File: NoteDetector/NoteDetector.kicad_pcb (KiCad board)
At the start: 2 copper layers, 25 x 25 mm, 24 parts, among them J1 Conn_02x03, J3 Conn_01x01, J4 Conn_01x01, Q1 Q_NMOS_DGS, U1 VM1010, U2 OPAMP, U3 ATtiny1614-SS

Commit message: save work: new layout almost done
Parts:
- removed U3: ATtiny1614-SS, Package_SO:SOIC-14_3.9x8.7mm_P1.27mm
- added C10: 22p, Capacitor_SMD:C_0603_1608Metric, F.Cu at (-3.86, 8.70)
- added C11: 100n, Capacitor_SMD:C_0603_1608Metric, F.Cu at (8.65, 5.25)
- added C12: 10n, Capacitor_SMD:C_0603_1608Metric, F.Cu at (7.15, 5.25)
- added C13: 1u, Capacitor_SMD:C_0603_1608Metric, F.Cu at (-0.75, -3.20)
- added C14: 1u, Capacitor_SMD:C_0603_1608Metric, F.Cu at (-0.75, -7.70)
- added C15: 1u, Capacitor_SMD:C_0603_1608Metric, F.Cu at (2.15, -2.00)
- added C8: 22p, Capacitor_SMD:C_0603_1608Metric, F.Cu at (-0.81, 9.82)
- added C9: 22p, Capacitor_SMD:C_0603_1608Metric, F.Cu at (-3.86, 5.70)
- added J2: Conn_01x01, TestPoint:TestPoint_Pad_D1.0mm, F.Cu at (10.5, 4.85)
- added J5: Conn_01x01, TestPoint:TestPoint_Loop_D2.50mm_Drill1.0mm, F.Cu at (-9.30, 6.40)
- added MK1: Microphone_Condenser, User:ElectretCondenserMic_SMT_MO063602-1, B.Cu at (0.00, 0.00)
- added Q2: Q_NMOS_DGS, Package_TO_SOT_SMD:SOT-23, F.Cu at (4.70, -6.00)
- added Q3: Q_NMOS_DGS, Package_TO_SOT_SMD:SOT-23, F.Cu at (-0.35, -10.2)
- added Q4: Q_NMOS_DGS, Package_TO_SOT_SMD:SOT-23, F.Cu at (3.55, -9.70)
- added R10: 10M, Resistor_SMD:R_0603_1608Metric, F.Cu at (-0.36, 1.12)
- added R11: 270k, Resistor_SMD:R_0603_1608Metric, F.Cu at (0.39, 3.38)
- added R12: 100, Resistor_SMD:R_0603_1608Metric, F.Cu at (5.80, 8.30)
- added R13: 10M, Resistor_SMD:R_0603_1608Metric, F.Cu at (3.39, 3.38)
- added R14: 10M, Resistor_SMD:R_0603_1608Metric, F.Cu at (0.69, 9.82)
- added R15: 270k, Resistor_SMD:R_0603_1608Metric, F.Cu at (-3.14, 11.0)
- added R16: 270k, Resistor_SMD:R_0603_1608Metric, F.Cu at (-2.36, 5.70)
- added R17: 270k, Resistor_SMD:R_0603_1608Metric, F.Cu at (-2.36, 8.70)
- added R18: R, Resistor_SMD:R_0603_1608Metric, F.Cu at (-0.75, -4.70)
- added R19: R, Resistor_SMD:R_0603_1608Metric, F.Cu at (-0.75, -6.20)
- added R20: R, Resistor_SMD:R_0603_1608Metric, F.Cu at (2.15, -5.00)
- C1, C4: value 100n -> 1n
- C2: value 1.5n -> 1n
- C3: value C -> 1n
- C5: value 47p -> 100n
- C6: value 100n -> 10n
- C7: value 10n -> 22p
- D1: moved to B.Cu
- J1: value Conn_02x03 -> Conn_01x05; footprint Connector_PinSocket_2.54mm:PinSocket_2x03_P2.54mm_Vertical -> Connector_PinHeader_1.27mm:PinHeader_2x03_P1.27mm_Vertical
- J3: footprint TestPoint:TestPoint_Loop_D2.50mm_Drill1.0mm -> TestPoint:TestPoint_Pad_D1.0mm
- R1: value 18k -> 1k
- R2, R3: value 10M -> 1k
- R5: value 10k -> 10M
- R6: value 1M -> 1k
- R7, R8, R9: value R -> 10M
- U1: value VM1010 -> OPAMP; footprint User:MEMS_mic_VS1010 -> Package_TO_SOT_SMD:SOT-23-5
- U2: value OPAMP -> PIC18F06; footprint Package_SO:SOIC-8_3.9x4.9mm_P1.27mm -> Package_SO:TSSOP-14_4.4x5mm_P0.65mm
- moved D1 26.5 mm to (0.00, -4.60), turned to 180 degrees
- moved R9 24.8 mm to (1.14, 1.12)
- moved J1 24.7 mm to (7.90, -0.74)
- moved C5 22.3 mm to (-2.61, 3.38), turned to 0 degrees
- moved C7 20.9 mm to (3.39, 1.88), turned to 180 degrees
- moved J3 20.4 mm to (-5.20, 0.55)
- moved R5 20.1 mm to (-5.34, 7.17), turned to 90 degrees
- moved Q1 19.5 mm to (4.65, -2.10), turned to -90 degrees
- moved R8 17.7 mm to (4.14, 8.62), turned to 90 degrees
- moved R7 17.3 mm to (4.14, 5.62), turned to 90 degrees
- moved R3 16.9 mm to (-2.61, 1.88), turned to 0 degrees
- moved C4 16.2 mm to (2.64, 8.62), turned to 90 degrees
- moved C2 15.8 mm to (-6.84, 7.17), turned to 90 degrees
- moved C1 15.5 mm to (-6.84, 4.17)
- moved R4 15.2 mm to (-5.34, 4.17)
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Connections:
- C1 pad 1: GND -> /Midscale2
- C2 pad 1: /Audio_raw -> Net-(C2-Pad1)
- C2 pad 2: Net-(C2-Pad2) -> /Midscale2
- C3 pad 1: Net-(C3-Pad1) -> /Midscale1
- C4 pad 1: GND -> Net-(C4-Pad1)
- C4 pad 2: +BATT -> /Midscale1
- C5 pad 1: /Audio_In -> /Audio_raw
- C6 pad 2: GND -> Net-(C6-Pad2)
- C7 pad 1: +BATT -> Net-(C7-Pad1)
- C7 pad 2: GND -> Net-(C7-Pad2)
- J1 pad 1: /UPDI -> /~{MCLR}
- J1 pad 3: unconnected-(J1-Pad3) -> GND
- J1 pad 4: unconnected-(J1-Pad4) -> /ICSP_DAT
- J1 pad 5: unconnected-(J1-Pad5) -> /ICSP_CLK
- J1 pad 6: GND -> unconnected-(J1-Pad6)
- J3 pad 1: /Audio_In -> /Audio_raw
- J4 pad 1: /Audio_raw -> +BATT
- Q1 pad 3: /AFE_gnd -> /gnd_switch
- R1 pad 1: Net-(R1-Pad1) -> /Audio_raw
- R1 pad 2: Net-(R1-Pad2) -> GND
- R2 pad 1: +BATT -> /gnd_switch
- R2 pad 2: Net-(C2-Pad2) -> Net-(C2-Pad1)
- R3 pad 1: Net-(C2-Pad2) -> /Audio_raw
- R3 pad 2: /AFE_gnd -> /gnd_switch
- R4 pad 1: Net-(C2-Pad2) -> /Midscale2
- R4 pad 2: Net-(C3-Pad1) -> +BATT
- R5 pad 1: Net-(C2-Pad2) -> Net-(C2-Pad1)
- R5 pad 2: Net-(C5-Pad2) -> /Midscale2
- R6 pad 1: Net-(C5-Pad2) -> /gnd_switch
- R6 pad 2: /Audio_In -> Net-(C4-Pad1)
- R7 pad 1: Net-(D1-Pad4) -> /Midscale1
- R7 pad 2: /PWM1 -> +BATT
- R8 pad 1: Net-(D1-Pad3) -> Net-(C4-Pad1)
- R8 pad 2: /PWM2 -> /Midscale1
- R9 pad 1: Net-(D1-Pad2) -> +BATT
- R9 pad 2: /PWM3 -> Net-(C5-Pad2)
- U1 pad 1: /Audio_raw -> Net-(C8-Pad1)
- U1 pad 2: Net-(R1-Pad1) -> Net-(C6-Pad2)
- U1 pad 3: Net-(R1-Pad2) -> /Midscale1
- U1 pad 4: GND -> Net-(C7-Pad2)
- U1 pad 5: /Mic_En -> +BATT
- U2 pad 1: unconnected-(U2-Pad1) -> +BATT
- U2 pad 2: Net-(C2-Pad2) -> /Audio_In
- U2 pad 3: Net-(C3-Pad1) -> unconnected-(U2-Pad3)
- U2 pad 4: /AFE_gnd -> /~{MCLR}
- U2 pad 6: /Audio_In -> unconnected-(U2-Pad6)
- U2 pad 7: +BATT -> unconnected-(U2-Pad7)
- U2 pad 8: unconnected-(U2-Pad8) -> /PWM3
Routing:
- net /gnd_switch: track 0.00 -> 32.7 mm
- net /UPDI: track 20.2 -> 0.00 mm, vias 2 -> 0
- net /Mic_En: track 19.2 -> 0.00 mm
- net /Wake: track 15.5 -> 0.00 mm
- net Net-(C7-Pad1): track 0.00 -> 14.2 mm, vias 0 -> 2
- net +BATT: track 14.1 -> 26.8 mm, vias 5 -> 3
- net Net-(C2-Pad2): track 12.3 -> 0.00 mm
- net /Midscale2: track 0.00 -> 11.8 mm
- net /PWM2: track 4.24 -> 14.6 mm
- net /AFE_gnd: track 9.10 -> 0.00 mm
- net Net-(C3-Pad1): track 8.56 -> 0.00 mm
- net Net-(C6-Pad2): track 0.00 -> 8.42 mm, vias 0 -> 2
- net Net-(C8-Pad1): track 0.00 -> 6.34 mm
- net /Midscale1: track 0.00 -> 6.23 mm
- net Net-(R18-Pad2): track 0.00 -> 4.78 mm
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- added copper zone on B.Cu, net GND
- removed copper zone on F.Cu, net GND
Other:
- board size 25 x 25 mm -> 25.4 x 25.4 mm
- board text removed: "Amp audio"
- board text removed: "Gnd nc"
- board text removed: "Note detector Proto Rev 0.1 2/8/2022"
- board text removed: "Raw audio"
- board text removed: "V+ UPDI"
- board text removed: "nc nc"

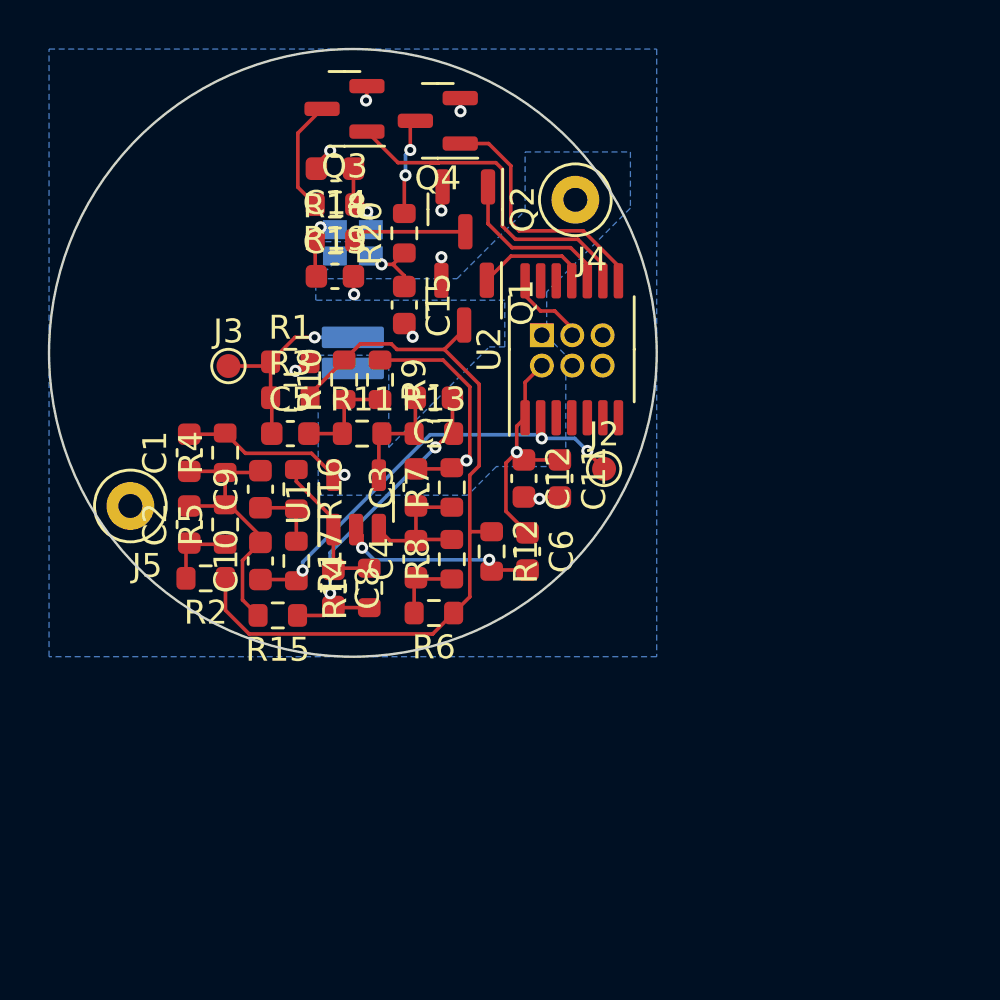
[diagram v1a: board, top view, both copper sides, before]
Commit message: rev2 board layout done
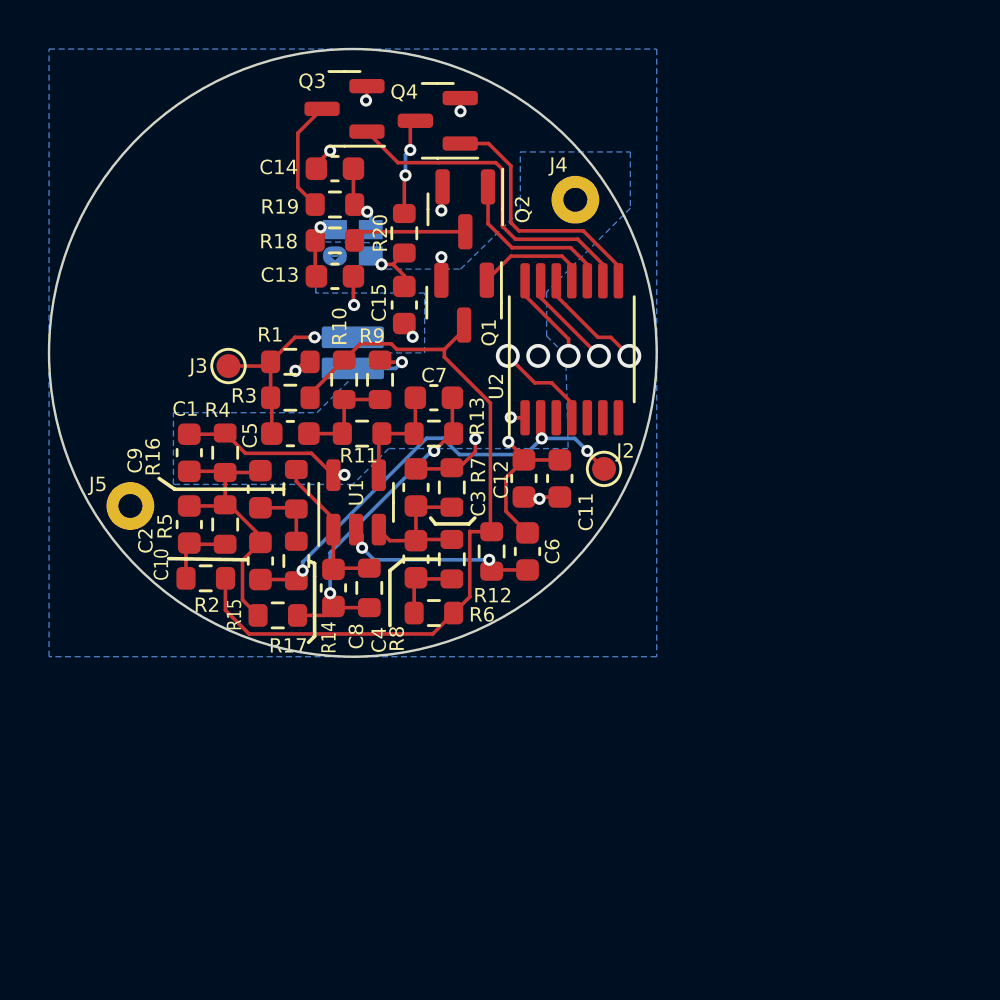
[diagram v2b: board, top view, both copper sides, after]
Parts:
- removed J1: Conn_01x05, Connector_PinHeader_1.27mm:PinHeader_2x03_P1.27mm_Vertical
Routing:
- net +BATT: track 26.8 -> 20.5 mm, vias 3 -> 6
- net /ICSP_CLK: track 0.00 -> 4.72 mm, vias 0 -> 1
- net /ICSP_DAT: track 0.00 -> 4.15 mm, vias 0 -> 1
- net /~{MCLR}: track 0.00 -> 4.11 mm, vias 0 -> 1
- net GND: track 11.4 -> 12.3 mm, vias 9 -> 10
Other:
- board text added: "+"

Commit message: Added revision to silkscreen
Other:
- board text added: "Matt Dion Lightup note detector Rev2 Feb 09 2023"
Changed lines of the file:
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@@
     (effects (font (size 1 1) (thickness 0.15)) (justify mirror))
+  )
+  (gr_text "Matt Dion\nLightup note detector\nRev2 Feb 09 2023" (at -8.75 -7.5 270) (layer "F.SilkS")
+    (effects (font (size 0.6 0.6) (thickness 0.1)) (justify left))
   )
   (segment (start 9.017 0.127) (end 9.017 -0.576652) (width 0.1524) (layer "F.Cu") (net 1))

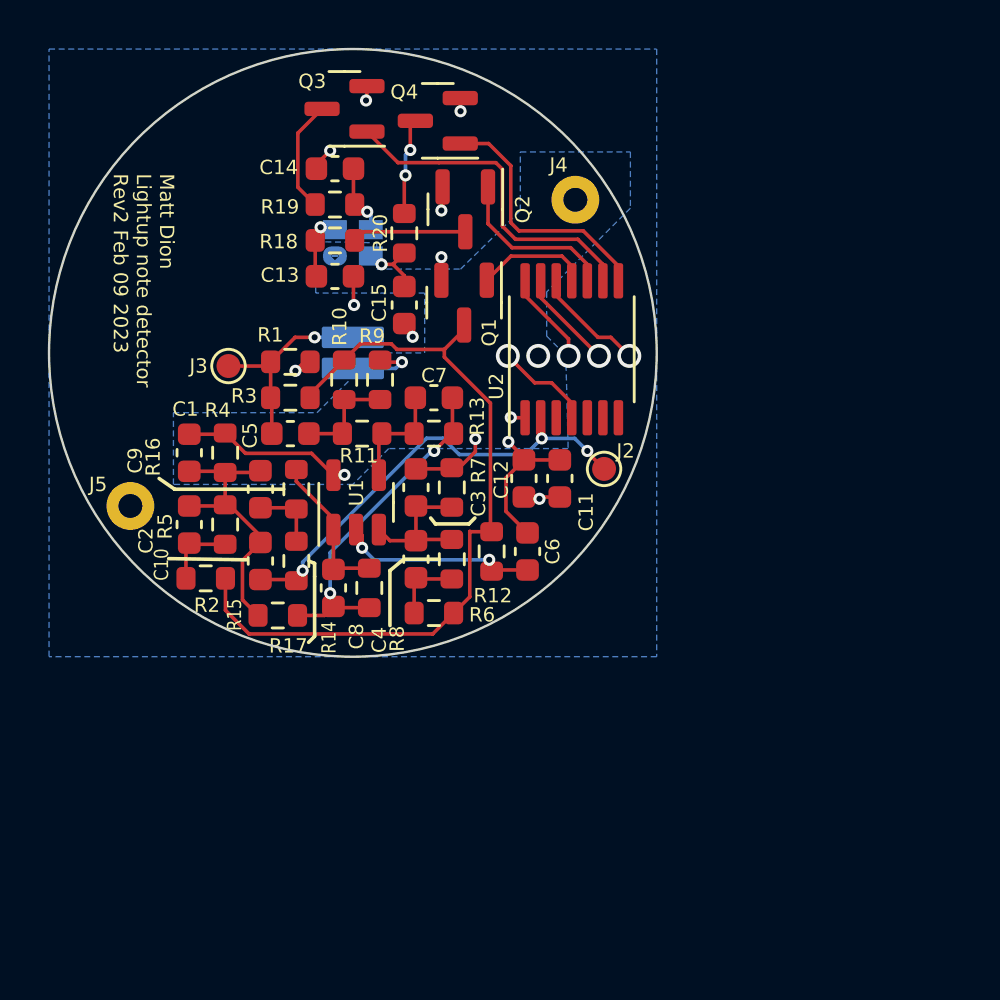
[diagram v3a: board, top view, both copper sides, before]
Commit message: Added programming bed PCB; moved PCB programming pads; added CR2032 battery holder; todo: fix silkscreen
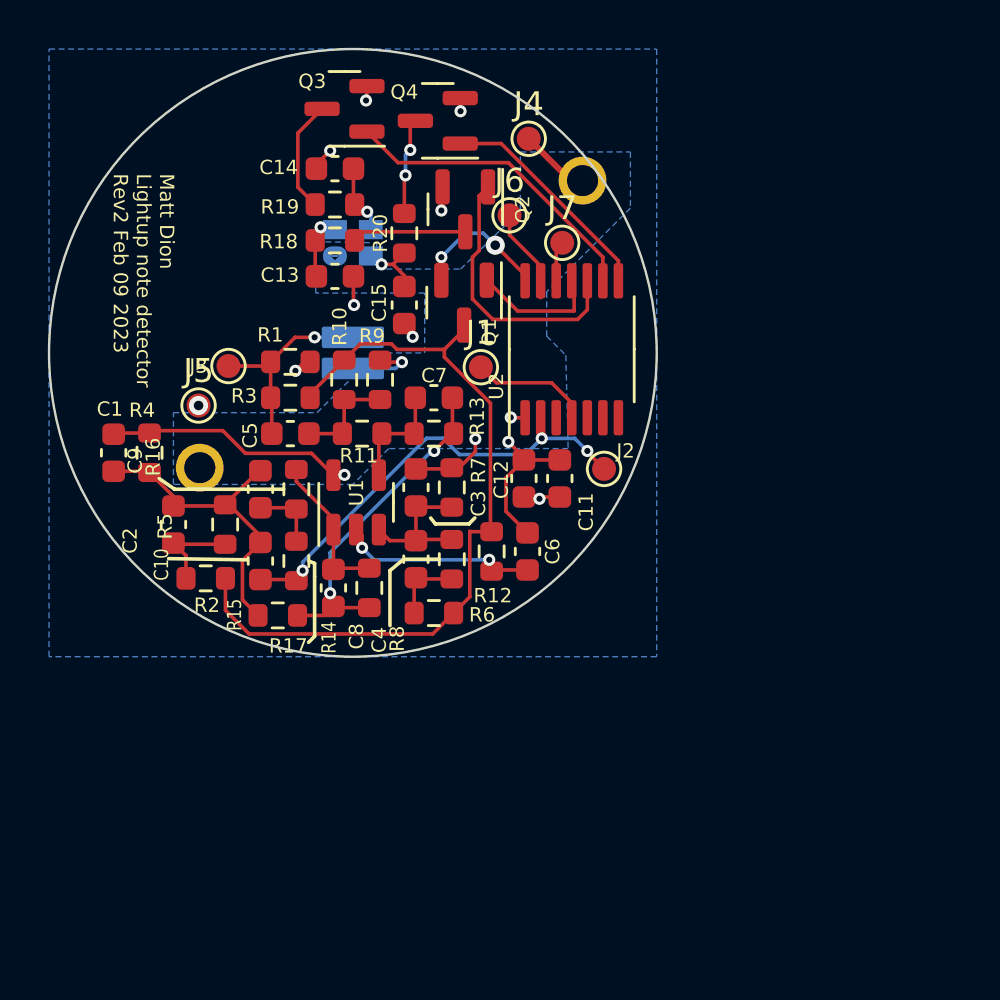
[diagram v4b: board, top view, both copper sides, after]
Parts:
- added BT1: CR2032Holder, User:BH-25C-1, F.Cu at (0.00, 0.00)
- added J1: Conn_01x01, TestPoint:TestPoint_Pad_D1.0mm, F.Cu at (5.35, 0.60)
- added J6: Conn_01x01, TestPoint:TestPoint_Pad_D1.0mm, F.Cu at (6.55, -5.75)
- added J7: Conn_01x01, TestPoint:TestPoint_Pad_D1.0mm, F.Cu at (8.75, -4.60)
- J4, J5: footprint TestPoint:TestPoint_Loop_D2.50mm_Drill1.0mm -> TestPoint:TestPoint_Pad_D1.0mm
- R18: value R -> 1k
- R19: value R -> 1.4k
- R20: value R -> 1.5k
- moved J5 5.08 mm to (-6.45, 2.20)
- moved J4 3.21 mm to (7.35, -8.95)
- moved C1 3.16 mm to (-10.0, 4.17)
- moved R4 3.16 mm to (-8.50, 4.17)
- moved C2 0.66 mm to (-7.50, 7.17)
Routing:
- net +BATT: track 20.5 -> 26.7 mm, vias 6 -> 5
- net /PWM1: track 7.08 -> 11.5 mm
- net /ICSP_CLK: track 4.72 -> 2.31 mm, vias 1 -> 0
- net /Midscale2: track 11.8 -> 13.5 mm
- net GND: track 12.3 -> 13.9 mm, vias 10 -> 11
- net /PWM2: track 14.2 -> 13.0 mm
- net /~{MCLR}: track 4.11 -> 5.04 mm, vias 1 -> 0
- net Net-(C2-Pad1): track 3.05 -> 3.87 mm
- net /AFE_En: track 4.76 -> 5.49 mm
- net /PWM3: track 10.7 -> 10.1 mm
- net /ICSP_DAT: track 4.15 -> 3.98 mm, vias 1 -> 0

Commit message: Updated BOM, moved programming pads outside of CR2032 battery holder coverage; board layout not finished
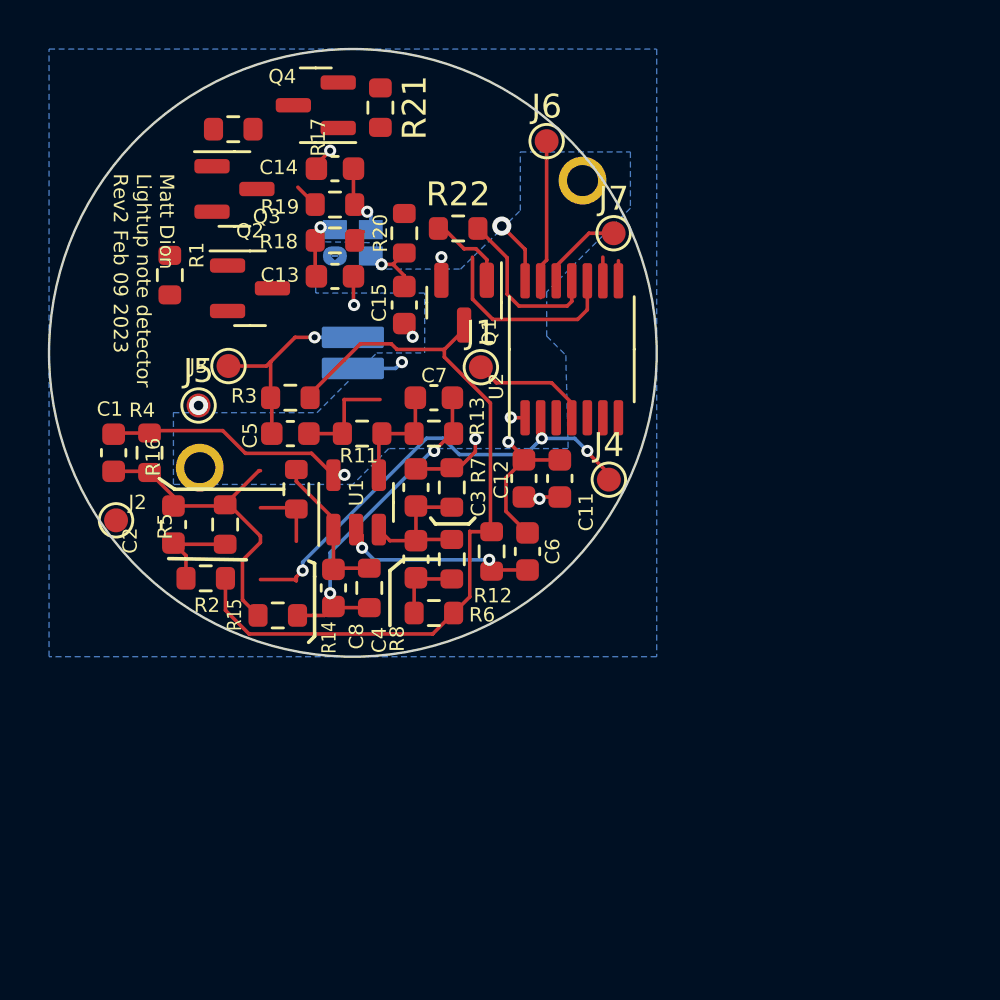
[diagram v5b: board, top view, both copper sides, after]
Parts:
- removed C10, C9: 22p, Capacitor_SMD:C_0603_1608Metric
- removed R10, R9: 10M, Resistor_SMD:R_0603_1608Metric
- added R21: 100, Resistor_SMD:R_0603_1608Metric, F.Cu at (1.15, -10.2)
- added R22: 100, Resistor_SMD:R_0603_1608Metric, F.Cu at (4.40, -5.20)
- C1, C2: value 1n -> 1u
- C5: value 100n -> C_in
- C7, C8: value 22p -> C_fb
- R1: value 1k -> 100
- R16: value 270k -> 1k
- R17: value 270k -> 100
- R3: value 1k -> 10k
- moved J2 20.5 mm to (-9.90, 7.00)
- moved R17 18.2 mm to (-5.00, -9.35), turned to 0 degrees
- moved J4 14.6 mm to (10.7, 5.30)
- moved Q2 9.59 mm to (-4.30, -2.70), turned to 0 degrees
- moved R1 6.21 mm to (-7.65, -3.25), turned to -90 degrees
- moved Q3 5.69 mm to (-4.95, -6.85), turned to 0 degrees
- moved Q4 5.14 mm to (-1.55, -10.3)
- moved J6 3.47 mm to (8.10, -8.85)
- moved J7 2.19 mm to (10.9, -5.00)
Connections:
- Q1 pad 1: /AFE_En -> Net-(Q1-Pad1)
- Q2 pad 1: /PWM1 -> Net-(Q2-Pad1)
- Q3 pad 1: /PWM2 -> Net-(Q3-Pad1)
- Q4 pad 1: /PWM3 -> Net-(Q4-Pad1)
- R1 pad 1: /Audio_raw -> Net-(Q2-Pad1)
- R1 pad 2: GND -> /PWM1
- R16 pad 2: Net-(C9-Pad1) -> /Audio_In
- R17 pad 1: Net-(C9-Pad1) -> Net-(Q3-Pad1)
- R17 pad 2: /Audio_In -> /PWM2
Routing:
- net /PWM2: track 13.0 -> 0.99 mm
- net /PWM3: track 10.1 -> 1.46 mm
- net GND: track 13.9 -> 8.73 mm, vias 11 -> 7
- net Net-(Q2-Pad3): track 4.78 -> 0.51 mm
- net Net-(Q4-Pad3): track 4.07 -> 0.00 mm, vias 2 -> 0
- net Net-(Q3-Pad3): track 4.72 -> 1.03 mm
- net Net-(Q1-Pad1): track 0.00 -> 3.42 mm
- net +BATT: track 26.7 -> 23.3 mm
- net /PWM1: track 11.5 -> 8.28 mm
- net /Audio_In: track 19.1 -> 22.0 mm
- net Net-(C9-Pad1): track 2.87 -> 0.00 mm
- net /ICSP_DAT: track 3.98 -> 6.64 mm
- net /ICSP_CLK: track 2.31 -> 4.20 mm
- net /AFE_En: track 5.49 -> 7.24 mm

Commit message: Rev 3 layout (hastily) completed!
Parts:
- moved J5 10.4 mm to (-8.90, -7.95)
- moved J2 6.97 mm to (-3.05, 8.30)
- moved Q4 4.52 mm to (2.55, -8.45), turned to -90 degrees
- moved R21 4.19 mm to (5.10, -8.85), turned to 90 degrees
- moved R1 1.60 mm to (-7.70, -4.85), turned to 90 degrees
- turned C13 to 180 degrees
- turned R18 to 180 degrees
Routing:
- net /PWM1: track 8.28 -> 28.5 mm, vias 0 -> 6
- net /PWM2: track 0.99 -> 20.3 mm, vias 0 -> 4
- net /PWM3: track 1.46 -> 8.67 mm, vias 0 -> 4
- net /Audio_In: track 22.0 -> 15.5 mm, vias 3 -> 2
- net Net-(C5-Pad2): track 4.36 -> 1.51 mm
- net Net-(Q2-Pad1): track 0.00 -> 2.59 mm
- net /Midscale2: track 13.5 -> 10.9 mm
- net Net-(Q2-Pad3): track 0.51 -> 2.74 mm
- net Net-(Q4-Pad3): track 0.00 -> 1.85 mm
- net Net-(Q4-Pad1): track 0.00 -> 1.72 mm
- net Net-(Q3-Pad3): track 1.03 -> 2.71 mm
- net Net-(Q3-Pad1): track 0.00 -> 1.58 mm
- net GND: track 8.73 -> 10.3 mm, vias 7 -> 10
- net /ICSP_DAT: track 6.64 -> 8.00 mm
- net /ICSP_CLK: track 4.20 -> 3.59 mm
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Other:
- board text added: "Gnd"
- board text added: "Matt Dion Lightup note detector Rev3 Mar 20 2023"
- board text added: "V+"
- board text removed: "Matt Dion Lightup note detector Rev2 Feb 09 2023"
